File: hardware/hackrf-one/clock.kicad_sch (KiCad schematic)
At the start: 48 parts, among them P1 AD_CLK, P16 CLKIN, P2 CLKOUT, P21 MIX_CLK, P37 SCL, P38 SDA, P57 XCVR_CLK, P59 GCK2, P60 SGPIO_CLK, P72 GP_CLKIN, P8 FSX2_CLK, U16 74LVC1G3157, U19 Si5351A-B-GT, U22 74LVC1G80, U26 74AUP2G58GU, U27 74AUP2G58GU, U28 74AUP2G58GU, X1 GSG-XTAL4PIN

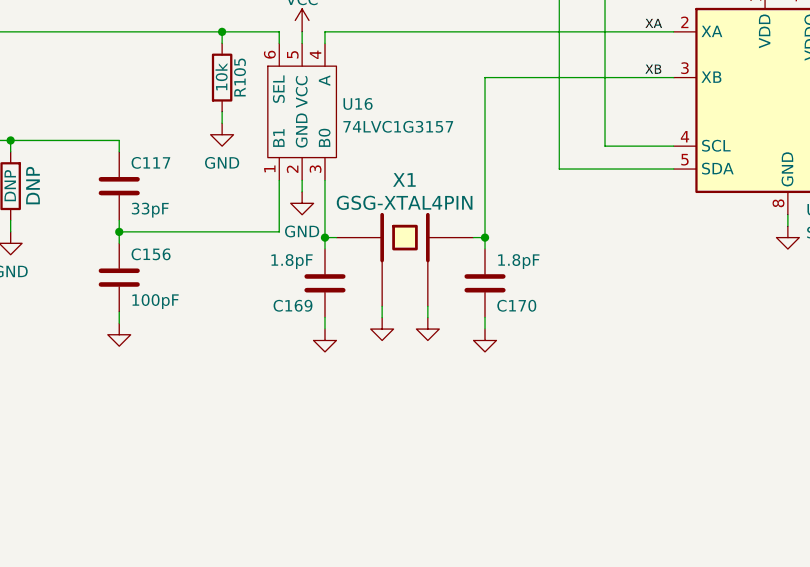
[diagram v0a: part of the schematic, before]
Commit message: HackRF One: component selections, DNP, and Notes
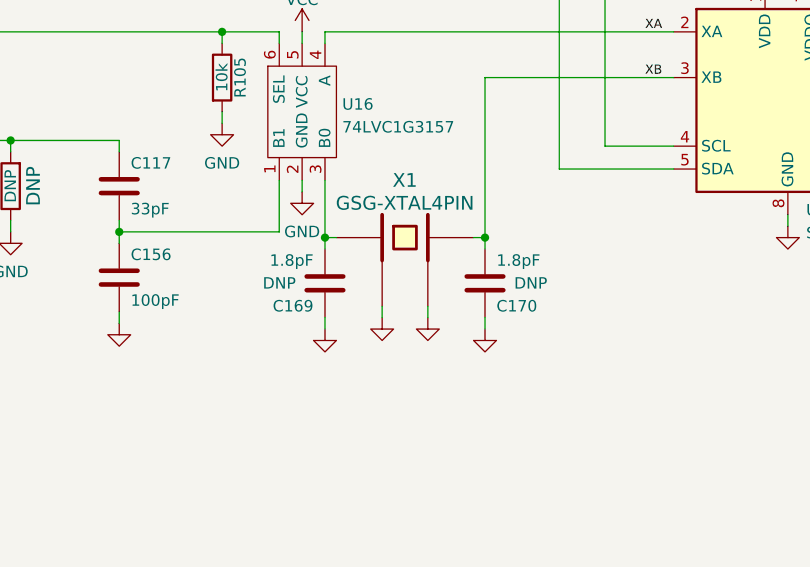
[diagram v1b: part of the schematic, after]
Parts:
- C117: Manufacturer Murata -> Samsung; Part Number GRM1555C1H330JA01D -> CL05C330JB5NNNC
- C156: Manufacturer Murata -> Samsung; Part Number GRM1555C1H101JA01D -> CL05C101JB5NNNC
- C169, C170: DNP (none) -> DNP; Manufacturer Murata -> (none); Part Number GRM1555C1E1R8BA01D -> (none)
- P1, P21, P37, P38, P57, P59, P60, P72, P8, R40: DNP (none) -> DNP; Note DNP -> (none)
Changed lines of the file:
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@@
       (effects (font (size 1.524 1.524)) hide)
     )
-    (property "Note" "DNP" (id 4) (at 205.105 66.675 0)
+    (property "DNP" "DNP" (id 4) (at 205.105 66.675 0)
       (effects (font (size 1.524 1.524)) hide)
     )
@@
       (effects (font (size 1.524 1.524)) hide)
     )
-    (property "Note" "DNP" (id 4) (at 208.915 66.675 0)
+    (property "DNP" "DNP" (id 4) (at 208.915 66.675 0)
       (effects (font (size 1.524 1.524)) hide)
     )
@@
       (effects (font (size 1.524 1.524)))
     )
-    (property "Manufacturer" "Murata" (id 4) (at 186.69 112.395 0)
-      (effects (font (size 1.524 1.524)) hide)
-    )
-    (property "Part Number" "GRM1555C1E1R8BA01D" (id 5) (at 186.69 112.395 0)
-      (effects (font (size 1.524 1.524)) hide)
-    )
-    (property "Description" "CAP CER 1.8PF 25V C0G/NP0 0402" (id 6) (at 186.69 112.395 0)
-      (effects (font (size 1.524 1.524)) hide)
-    )
+    (property "Manufacturer" "" (id 4) (at 186.69 112.395 0)
+      (effects (font (size 1.524 1.524)) hide)
+    )
+    (property "Part Number" "" (id 5) (at 186.69 112.395 0)
+      (effects (font (size 1.524 1.524)) hide)
+    )
+    (property "Description" "" (id 6) (at 186.69 112.395 0)
+      (effects (font (size 1.524 1.524)) hide)
+    )
+    (property "DNP" "DNP" (id 7) (at 181.61 112.395 0))
     (pin "1")
     (pin "2")
@@
       (effects (font (size 1.524 1.524)))
     )
-    (property "Manufacturer" "Murata" (id 4) (at 204.47 112.395 0)
-      (effects (font (size 1.524 1.524)) hide)
-    )
-    (property "Part Number" "GRM1555C1E1R8BA01D" (id 5) (at 204.47 112.395 0)
-      (effects (font (size 1.524 1.524)) hide)
-    )
-    (property "Description" "CAP CER 1.8PF 25V C0G/NP0 0402" (id 6) (at 204.47 112.395 0)
-      (effects (font (size 1.524 1.524)) hide)
-    )
+    (property "Manufacturer" "" (id 4) (at 204.47 112.395 0)
+      (effects (font (size 1.524 1.524)) hide)
+    )
+    (property "Part Number" "" (id 5) (at 204.47 112.395 0)
+      (effects (font (size 1.524 1.524)) hide)
+    )
+    (property "Description" "" (id 6) (at 204.47 112.395 0)
+      (effects (font (size 1.524 1.524)) hide)
+    )
+    (property "DNP" "DNP" (id 7) (at 209.55 112.395 0))
     (pin "1")
     (pin "2")
@@
       (effects (font (size 1.524 1.524)) hide)
     )
-    (property "Note" "DNP" (id 4) (at 69.85 190.5 0)
+    (property "DNP" "DNP" (id 4) (at 69.85 190.5 0)
       (effects (font (size 1.524 1.524)) hide)
     )
@@
       (effects (font (size 1.524 1.524)) hide)
     )
-    (property "Note" "DNP" (id 4) (at 268.605 67.945 0)
+    (property "DNP" "DNP" (id 4) (at 268.605 67.945 0)
       (effects (font (size 1.524 1.524)) hide)
     )
@@
       (effects (font (size 1.524 1.524)) hide)
     )
-    (property "Note" "DNP" (id 4) (at 62.23 190.5 0)
+    (property "DNP" "DNP" (id 4) (at 62.23 190.5 0)
       (effects (font (size 1.524 1.524)) hide)
     )
@@
       (effects (font (size 1.524 1.524)))
     )
-    (property "Note" "DNP" (id 4) (at 154.305 101.6 90)
+    (property "DNP" "DNP" (id 4) (at 154.305 101.6 90)
       (effects (font (size 1.524 1.524)))
     )
@@
       (effects (font (size 1.524 1.524)) hide)
     )
-    (property "Note" "DNP" (id 4) (at 46.99 190.5 0)
+    (property "DNP" "DNP" (id 4) (at 46.99 190.5 0)
       (effects (font (size 1.524 1.524)) hide)
     )
@@
       (effects (font (size 1.524 1.524)) hide)
     )
-    (property "Note" "DNP" (id 4) (at 50.8 190.5 0)
+    (property "DNP" "DNP" (id 4) (at 50.8 190.5 0)
       (effects (font (size 1.524 1.524)) hide)
     )
@@
       (effects (font (size 1.524 1.524)) hide)
     )
-    (property "Manufacturer" "Murata" (id 4) (at 452.12 44.45 0)
-      (effects (font (size 1.524 1.524)) hide)
-    )
-    (property "Part Number" "GRM1555C1H330JA01D" (id 5) (at 452.12 44.45 0)
-      (effects (font (size 1.524 1.524)) hide)
-    )
-    (property "Description" "CAP CER 33PF 50V 5% NP0 0402" (id 6) (at 452.12 44.45 0)
+    (property "Manufacturer" "Samsung" (id 4) (at 452.12 44.45 0)
+      (effects (font (size 1.524 1.524)) hide)
+    )
+    (property "Part Number" "CL05C330JB5NNNC" (id 5) (at 452.12 44.45 0)
+      (effects (font (size 1.524 1.524)) hide)
+    )
+    (property "Description" "CAP CER 33PF 50V 5% C0G/NP0 0402" (id 6) (at 452.12 44.45 0)
       (effects (font (size 1.524 1.524)) hide)
     )
@@
       (effects (font (size 1.524 1.524)) hide)
     )
-    (property "Note" "DNP" (id 4) (at 290.195 147.32 0)
+    (property "DNP" "DNP" (id 4) (at 290.195 147.32 0)
       (effects (font (size 1.524 1.524)) hide)
     )
@@
       (effects (font (size 1.524 1.524)) hide)
     )
-    (property "Manufacturer" "Murata" (id 4) (at 240.03 72.39 0)
-      (effects (font (size 1.524 1.524)) hide)
-    )
-    (property "Part Number" "GRM1555C1H101JA01D" (id 5) (at 240.03 72.39 0)
-      (effects (font (size 1.524 1.524)) hide)
-    )
-    (property "Description" "CAP CER 100PF 50V 5% NP0 0402" (id 6) (at 240.03 72.39 0)
+    (property "Manufacturer" "Samsung" (id 4) (at 240.03 72.39 0)
+      (effects (font (size 1.524 1.524)) hide)
+    )
+    (property "Part Number" "CL05C101JB5NNNC" (id 5) (at 240.03 72.39 0)
+      (effects (font (size 1.524 1.524)) hide)
+    )
+    (property "Description" "CAP CER 100PF 50V 5% C0G/NP0 0402" (id 6) (at 240.03 72.39 0)
       (effects (font (size 1.524 1.524)) hide)
     )
@@
       (effects (font (size 1.524 1.524)) hide)
     )
-    (property "Note" "DNP" (id 4) (at 58.42 190.5 0)
-      (effects (font (size 1.524 1.524)) hide)
-    )
+    (property "DNP" "DNP" (id 4) (at 58.42 190.5 0)
+      (effects (font (size 1.524 1.524)) hide)
+    )

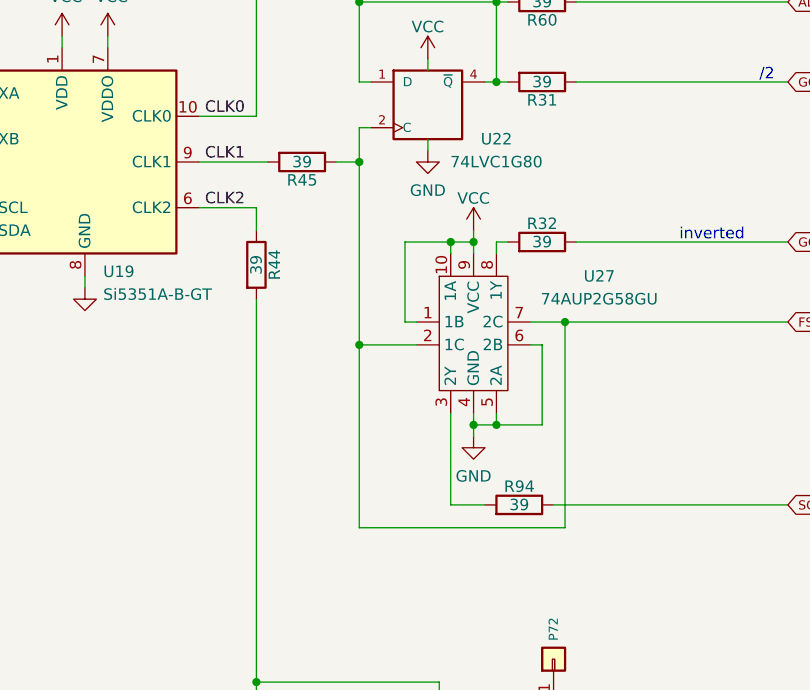
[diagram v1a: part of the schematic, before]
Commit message: HackRF One: chain SGPIO_CLK and GCK2 buffers
This more closely emulates the clock phase relationships on prior
hardware revisions that used the Si5351C.

Update clock trace widths.
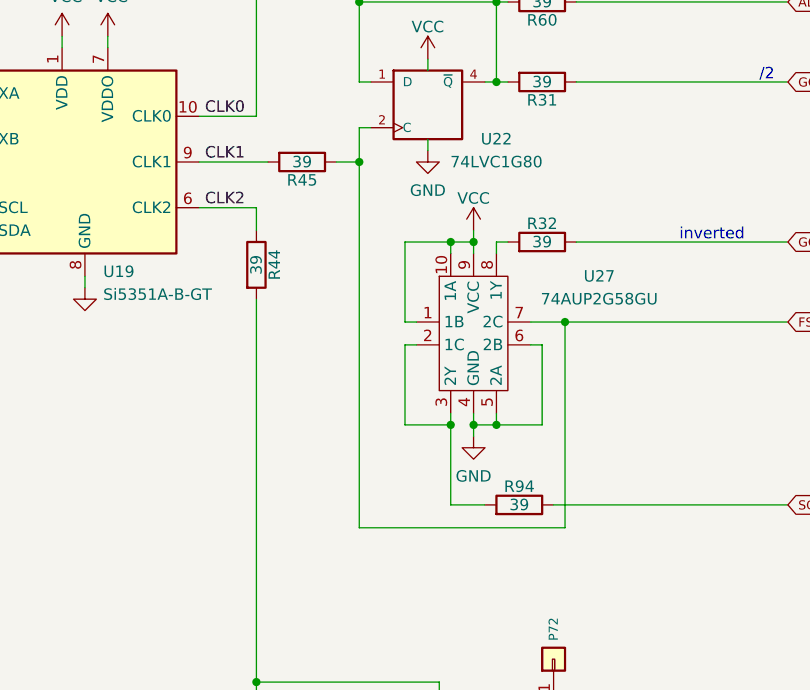
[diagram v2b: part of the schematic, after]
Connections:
- net FSX2_CLK: no longer U27.2 (1C)
- net at R94.2, U27.3 (2Y): now also U27.2 (1C)
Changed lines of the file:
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@@
   (junction (at 278.765 100.965) (diameter 0) (color 0 0 0 0)
   )
+  (junction (at 278.765 121.285) (diameter 0) (color 0 0 0 0)
+  )
   (junction (at 291.465 109.855) (diameter 0) (color 0 0 0 0)
   )
@@
   (junction (at 111.125 228.6) (diameter 0) (color 0 0 0 0)
   )
-  (junction (at 268.605 112.395) (diameter 0) (color 0 0 0 0)
-  )
   (junction (at 80.645 228.6) (diameter 0) (color 0 0 0 0)
   )
@@
     (stroke (width 0) (type default) (color 0 0 0 0))
   )
-  (wire (pts (xy 278.765 120.015) (xy 278.765 130.175))
+  (wire (pts (xy 278.765 120.015) (xy 278.765 121.285))
     (stroke (width 0) (type default) (color 0 0 0 0))
   )
@@
     (stroke (width 0) (type default) (color 0 0 0 0))
   )
-  (wire (pts (xy 268.605 132.715) (xy 268.605 112.395))
+  (wire (pts (xy 268.605 92.075) (xy 268.605 132.715))
     (stroke (width 0) (type default) (color 0 0 0 0))
   )
@@
     (stroke (width 0) (type default) (color 0 0 0 0))
   )
+  (wire (pts (xy 274.955 112.395) (xy 273.685 112.395))
+    (stroke (width 0) (type default) (color 0 0 0 0))
+  )
   (wire (pts (xy 101.6 87.63) (xy 101.6 90.17))
     (stroke (width 0) (type default) (color 0 0 0 0))
@@
     (stroke (width 0) (type default) (color 0 0 0 0))
   )
-  (wire (pts (xy 268.605 92.075) (xy 268.605 112.395))
-    (stroke (width 0) (type default) (color 0 0 0 0))
-  )
   (wire (pts (xy 131.445 118.11) (xy 131.445 116.84))
     (stroke (width 0) (type default) (color 0 0 0 0))
@@
     (stroke (width 0) (type default) (color 0 0 0 0))
   )
-  (wire (pts (xy 274.955 112.395) (xy 268.605 112.395))
-    (stroke (width 0) (type default) (color 0 0 0 0))
-  )
   (wire (pts (xy 140.335 87.63) (xy 121.285 87.63))
     (stroke (width 0) (type default) (color 0 0 0 0))
@@
     (stroke (width 0) (type default) (color 0 0 0 0))
   )
+  (wire (pts (xy 273.685 112.395) (xy 273.685 121.285))
+    (stroke (width 0) (type default) (color 0 0 0 0))
+  )
   (wire (pts (xy 283.845 120.015) (xy 283.845 121.285))
     (stroke (width 0) (type default) (color 0 0 0 0))
@@
     (stroke (width 0) (type default) (color 0 0 0 0))
   )
+  (wire (pts (xy 273.685 121.285) (xy 278.765 121.285))
+    (stroke (width 0) (type default) (color 0 0 0 0))
+  )
   (wire (pts (xy 111.125 220.98) (xy 121.285 220.98))
     (stroke (width 0) (type default) (color 0 0 0 0))
@@
     (stroke (width 0) (type default) (color 0 0 0 0))
   )
+  (wire (pts (xy 278.765 121.285) (xy 278.765 130.175))
+    (stroke (width 0) (type default) (color 0 0 0 0))
+  )

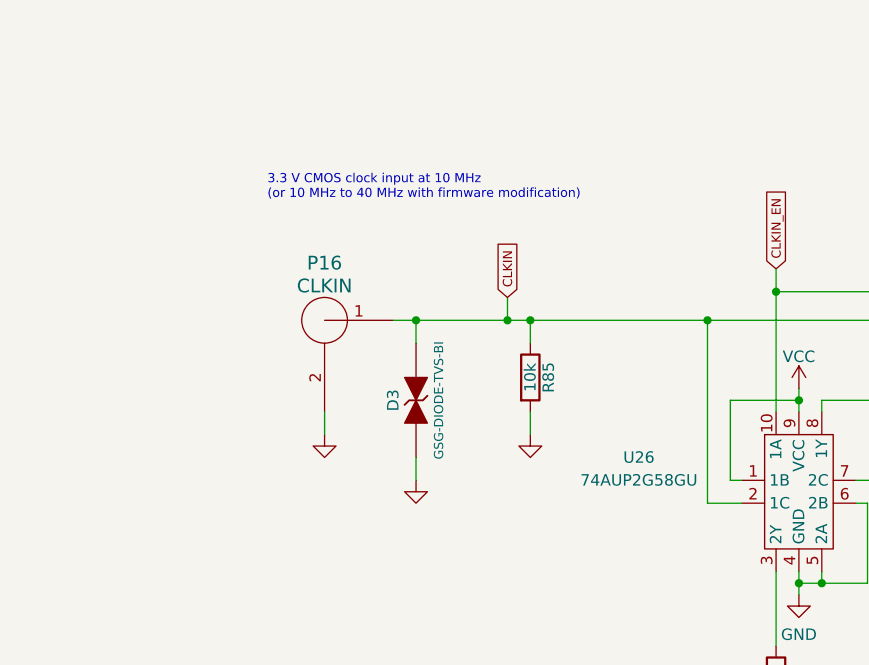
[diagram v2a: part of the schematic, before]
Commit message: HackRF One: AC couple CLKIN
We've always specified that CLKIN should be DC (based on the Si5351C
documentation), but it has worked with AC input.  AC coupling the buffer
input restores this undocumented feature.
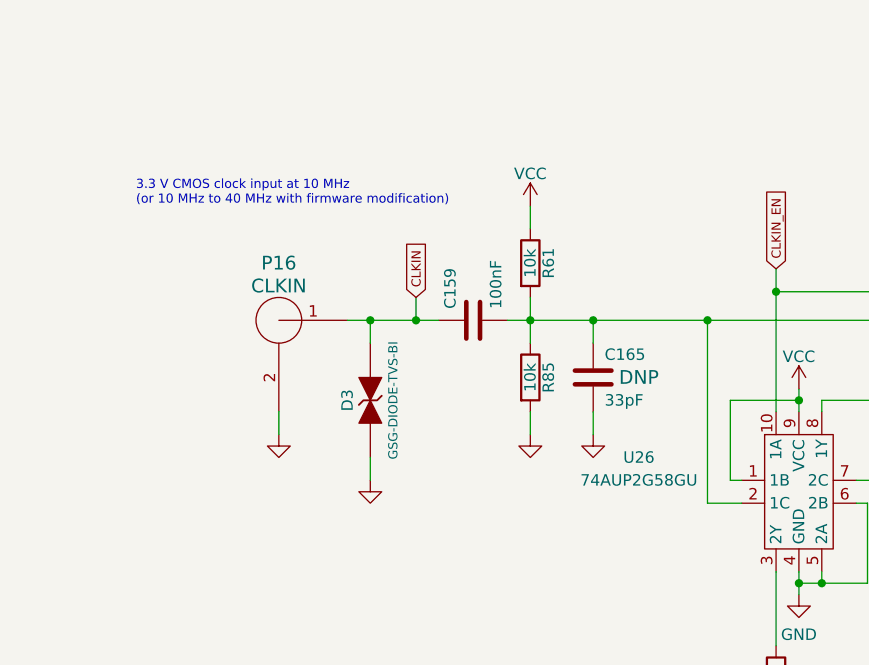
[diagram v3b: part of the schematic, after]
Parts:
- added C159: 100nF, hackrf:GSG-0402, symbol Device:C
- added C165: 33pF, hackrf:GSG-0402, symbol Device:C
- added R61: 10k, hackrf:GSG-0402, symbol Device:R
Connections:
- net CLKIN: now also C159.1; no longer R85.1, U26.2 (1C), U26.7 (2C)
- net GND: now also C165.2
- net VCC: now also R61.1
- new net: C159.2, C165.1, R61.2, R85.1, U26.2 (1C), U26.7 (2C)
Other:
- moved on the sheet: D3, P16
